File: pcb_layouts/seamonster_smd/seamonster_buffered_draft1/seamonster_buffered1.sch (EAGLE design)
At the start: 84 parts, among them IC1 7805T, IC2 4051D, IC3 4051D, IC4 DG408DY, IC5 4040D, IC6 40106D, IC7 4070D, Q1 THONKICONNNEW, Q2 THONKICONNNEW, Q3 THONKICONNNEW, Q4 THONKICONNNEW, Q5 THONKICONNNEW, Q6 THONKICONNNEW, SW1 T-80-T-SPDT-ON-OFF-ON, SW2 T-80-T-SPDT-ON-OFF-ON, SW3 T-80-T-SPDT-ON-OFF-ON, SW4 T-80-T-SPDT-ON-OFF-ON

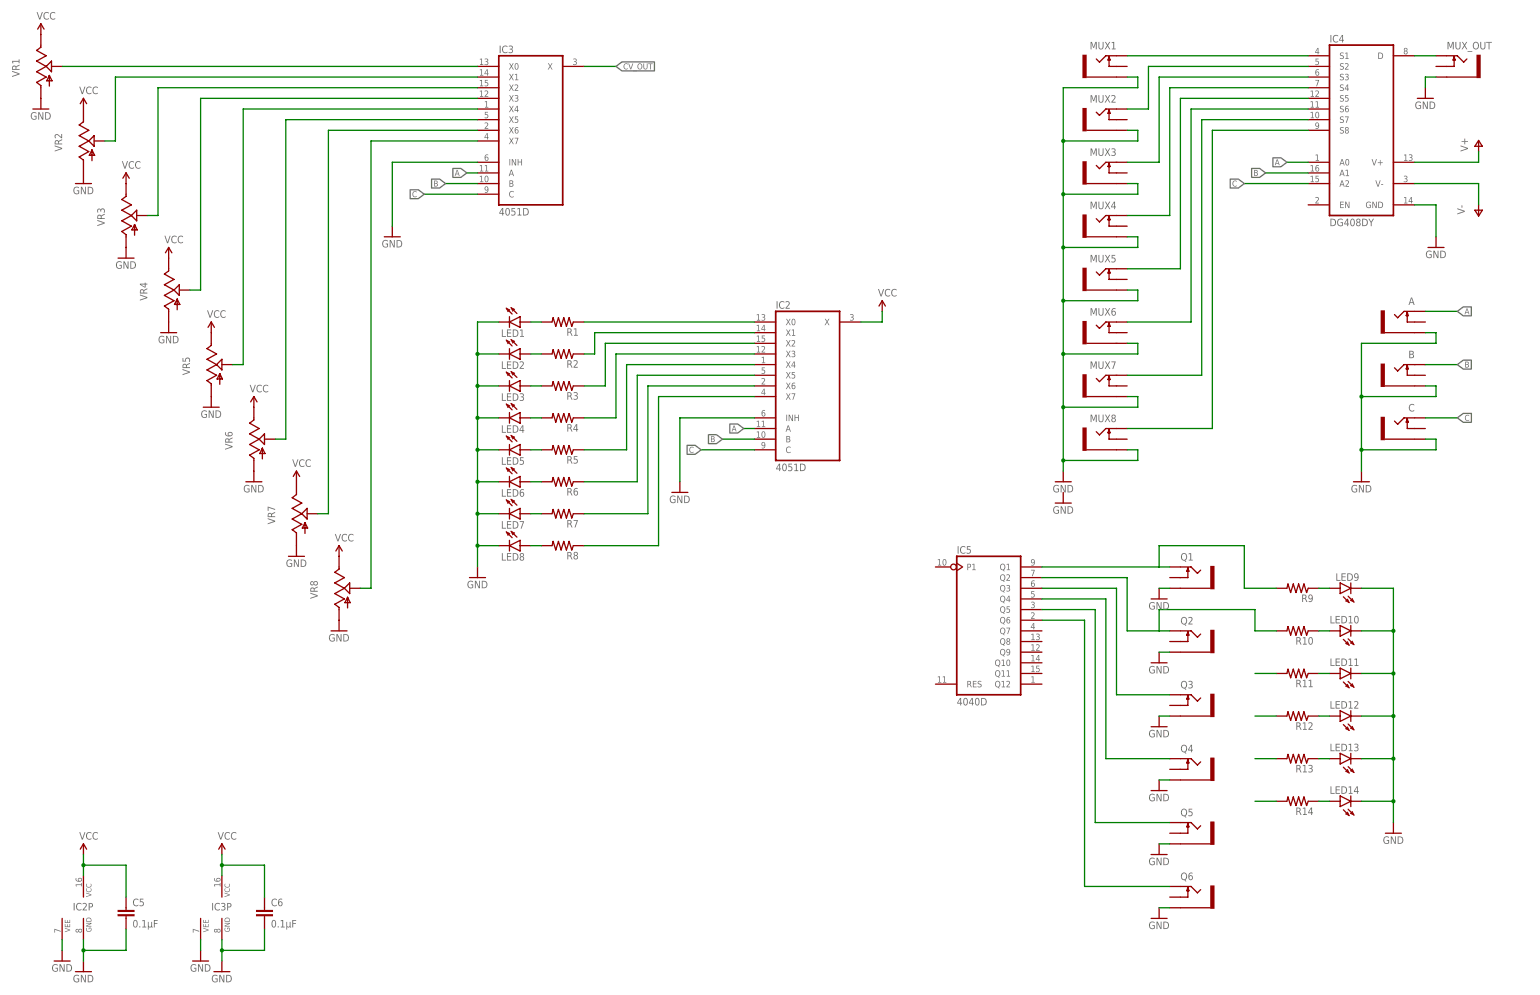
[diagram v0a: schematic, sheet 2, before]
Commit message: figured out invoking across multiple sheets
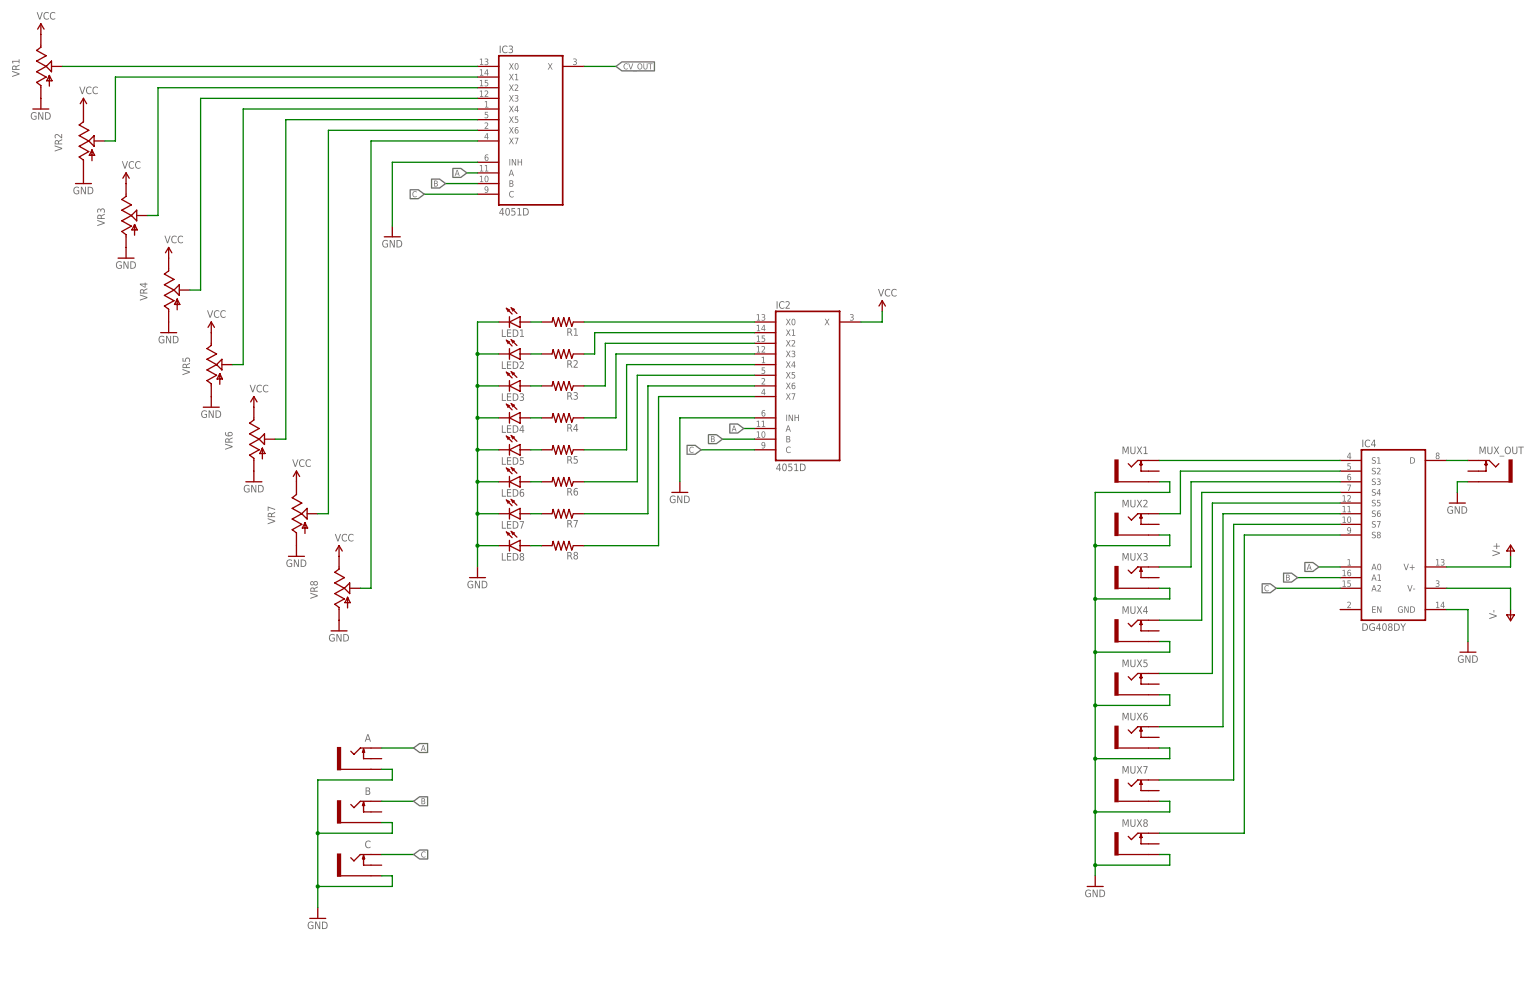
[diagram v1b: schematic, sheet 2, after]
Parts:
- removed IC5: 4040D, 40xx:4040D
- removed LED10, LED11, LED12, LED13, LED14, LED9: (no value), SparkFun-LED:LED3MM
- removed Q1, Q2, Q3, Q4, Q5, Q6: THONKICONNNEW, MusicThingModular:THONKICONNNEW
- removed R10, R11, R12, R13, R14, R9: (no value), SparkFun-Resistors:RESISTOR0805-RES
- added U1: TL084, MusicThingModular:TL074_SMD
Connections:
- removed net N$34: LED9.A, R9.1
- removed net N$35: LED10.A, R10.1
- removed net N$36: LED11.A, R11.1
- removed net N$37: LED12.A, R12.1
- removed net N$38: LED13.A, R13.1
- removed net N$39: LED14.A, R14.1
- removed net N$40: IC5A.Q1, Q1.TIP, R9.2
- removed net N$41: IC5A.Q2, Q2.TIP, R10.2
- removed net N$42: IC5A.Q3, Q3.TIP
- removed net N$43: IC5A.Q4, Q4.TIP
- removed net N$44: IC5A.Q5, Q5.TIP
- removed net N$45: IC5A.Q6, Q6.TIP
- removed net N$48: R11.2
- removed net N$49: R12.2
- removed net N$50: R13.2
- removed net N$51: R14.2
- new net CCO1_BUFFERED: U1A.-IN, U1A.OUT
- new net CCO2_BUFFERED: U1B.-IN, U1B.OUT
- new net CCO3_BUFFERED: U1C.-IN, U1C.OUT
- new net CCO4_BUFFERED: U1D.-IN, U1D.OUT
- net CCO1: now also U1A.+IN
- net GND: no longer IC2P.GND, IC2P.VEE, IC3P.GND, IC3P.VEE, LED10.C, LED11.C, LED12.C, LED13.C, LED14.C, LED9.C, Q1.SLEEVE, Q2.SLEEVE, Q3.SLEEVE, Q4.SLEEVE, Q5.SLEEVE, Q6.SLEEVE
- net N$54: now also U1B.+IN
- net N$57: now also U1C.+IN
- net N$61: now also U1D.+IN
- net V+: now also C5.1, U1P.V+
- net V-: now also C6.1, U1P.V-
- net VCC: no longer C5.1, C6.1, IC2P.VCC, IC3P.VCC
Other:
- moved on the sheet: A, B, C, C1, C2, C3, C4, IC1, IC4, IC6F, IC7A, IC7B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

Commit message: fleshed out schematic pages
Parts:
- added C15, C16, C17, C18, C19, C20: 0.1µF, SparkFun-Capacitors:CAP0805
- added IC5, IC8: 4046D, 40xx:4046D
- added U2: TL084, MusicThingModular:TL074_SMD
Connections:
- new net COMPLEX_OUT1_BUFFERED: U2A.-IN, U2A.OUT
- new net COMPLEX_OUT2_BUFFERED: U2B.-IN, U2B.OUT
- new net N$34: IC7A.I0
- new net N$35: IC7A.O, IC7B.I0
- new net N$36: IC7C.O, IC7D.I0
- new net N$37: IC7C.I0
- new net N$38: IC7B.O, U2A.+IN
- new net N$39: IC7D.O, U2B.+IN
- net CCO1_BUFFERED: now also IC7A.I1
- net CCO2_BUFFERED: now also IC7B.I1
- net CCO3_BUFFERED: now also IC7C.I1
- net CCO4_BUFFERED: now also IC7D.I1
- net GND: now also C15.2, C16.2, C17.2, C18.2, C19.2, C20.2, IC2P.GND, IC2P.VEE, IC3P.GND, IC3P.VEE, IC6P.VSS, IC7P.VSS
- net V+: now also C18.1, U2P.V+
- net V-: now also C19.1, U2P.V-
- net VCC: now also C15.1, C16.1, C17.1, C20.1, IC2P.VCC, IC3P.VCC, IC6P.VDD, IC7P.VDD

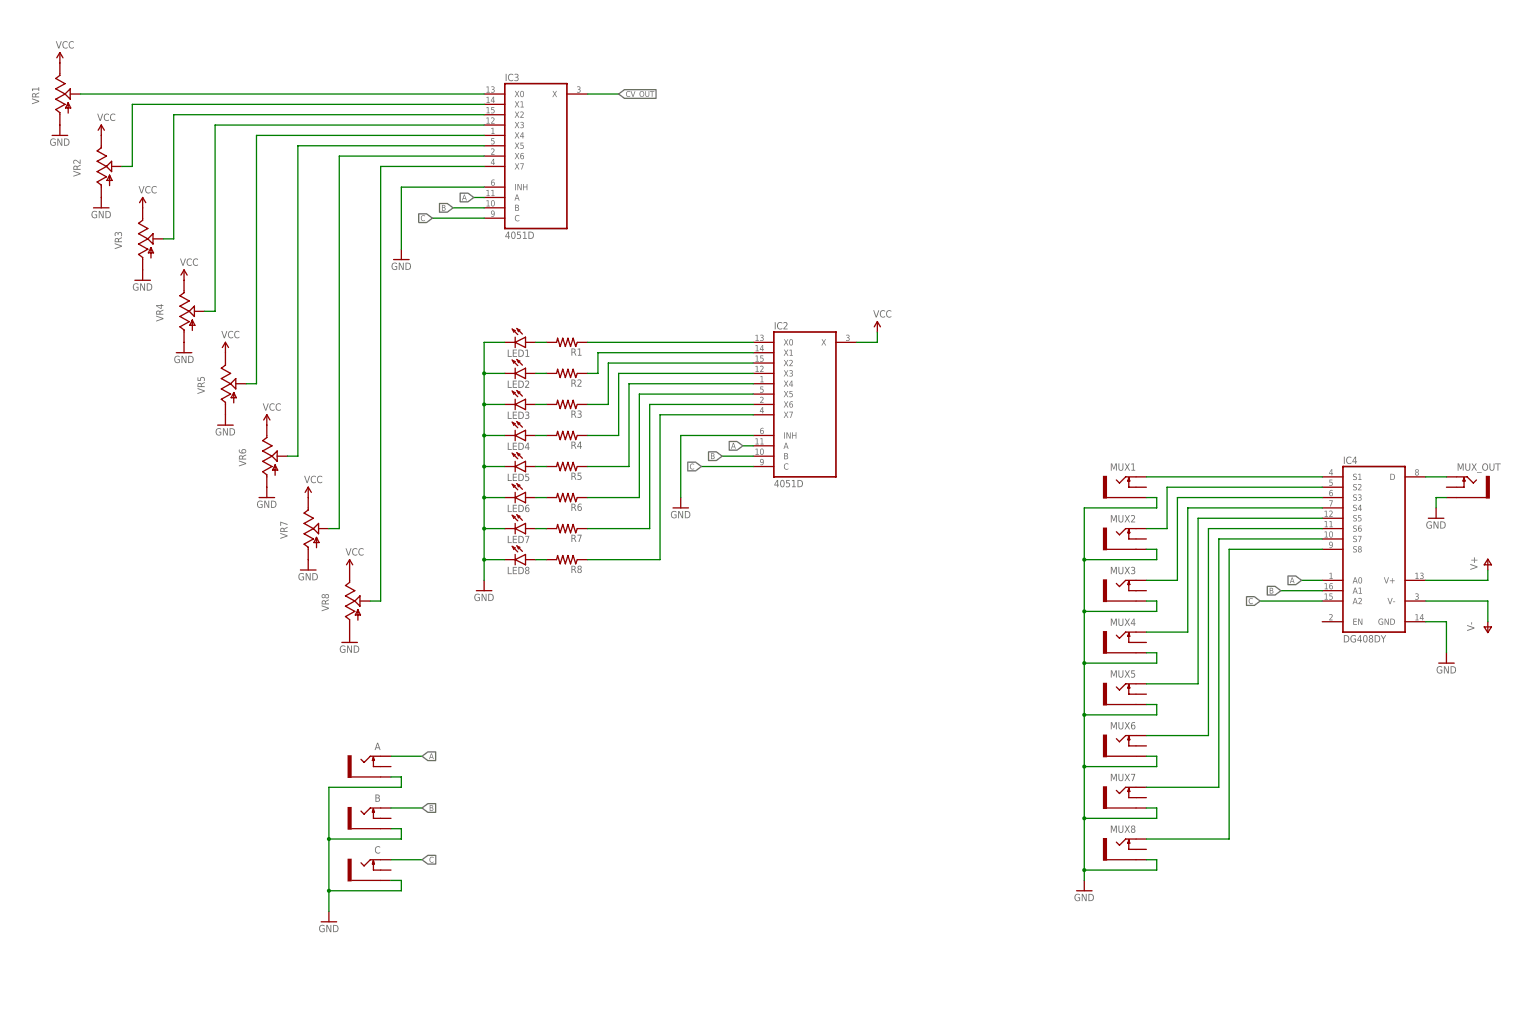
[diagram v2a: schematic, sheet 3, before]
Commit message: added in VCOs and more buffering
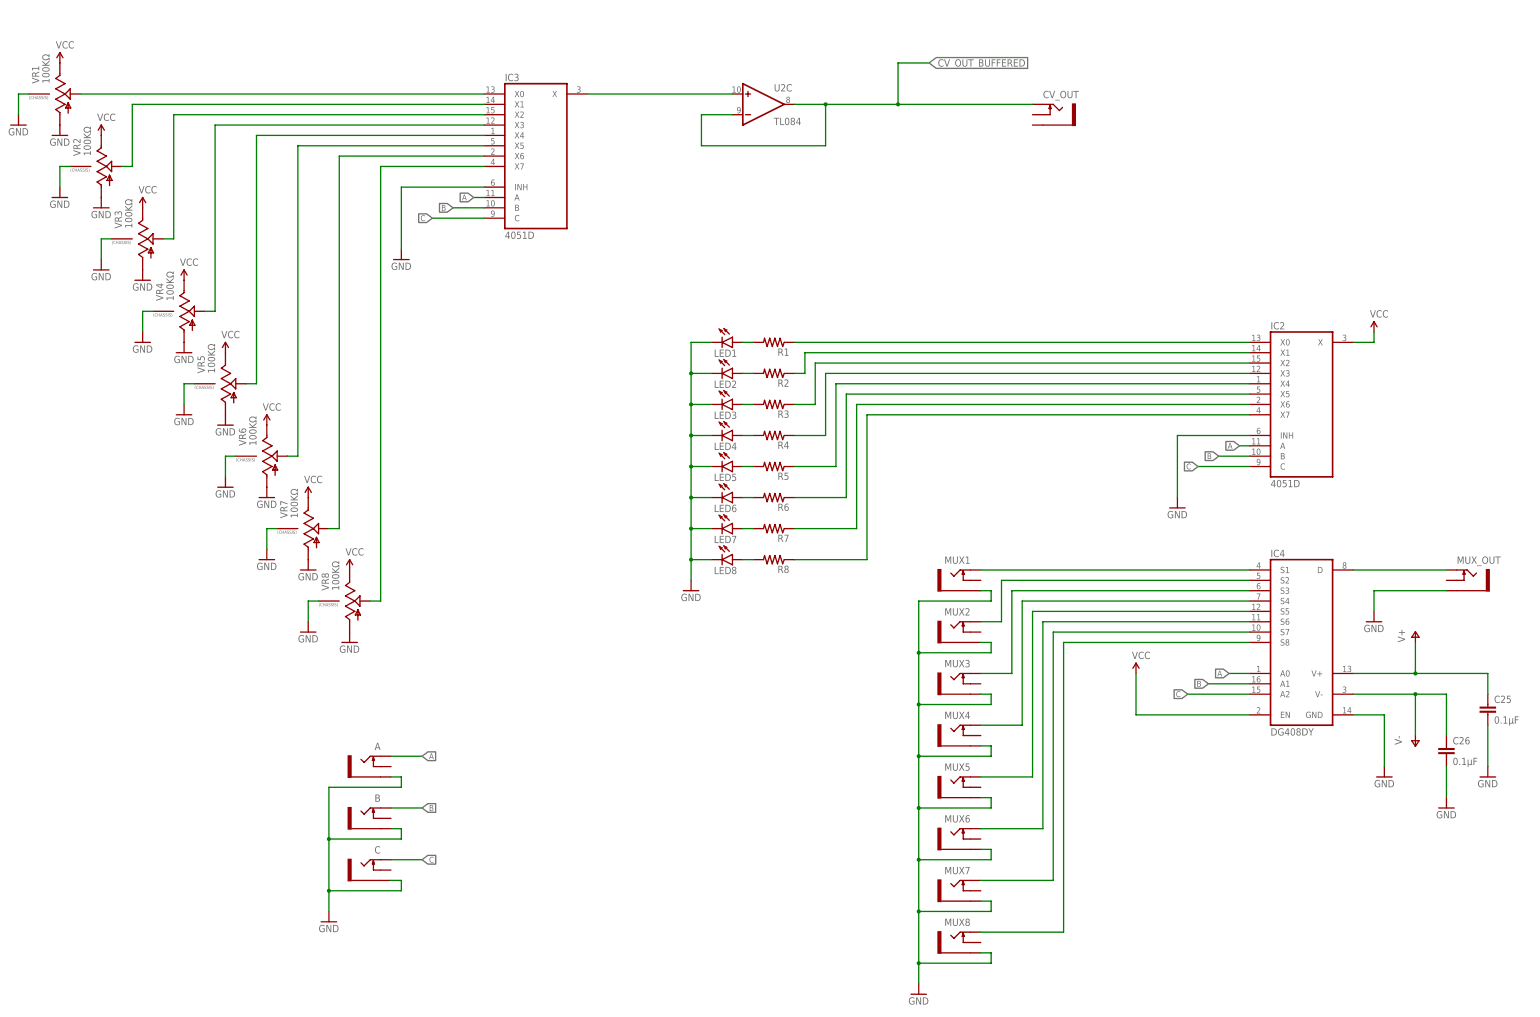
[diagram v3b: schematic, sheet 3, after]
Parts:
- added C21, C22, C25, C26, C27, C28, C29: 0.1µF, SparkFun-Capacitors:CAP0805
- added C23, C24: 1µF, SparkFun-Capacitors:CAP0805
- added CLOCK_IN, CV_OUT, Q1, Q2, Q3, Q4, Q5, Q6: THONKICONNNEW, MusicThingModular:THONKICONNNEW
- added CLOCK_SELECT: T-80-T-SPDT-ON-OFF-ON, MusicThingModular:T-80-T-SPDT-ON-OFF-ON
- added IC9: 4040D, 40xx:4040D
- added LED10, LED11, LED12, LED13, LED14, LED9: (no value), SparkFun-LED:LED3MM
- added R10, R11, R12, R13, R14, R15, R16, R17, R18, R9: (no value), SparkFun-Resistors:RESISTOR0805-RES
- added U3: TL084, MusicThingModular:TL074_SMD
- added VR13, VR14: 1MΩ, MusicThingModular:9MM_SNAP-IN_POT_CHASSIS
- added VR15: 100KΩ, MusicThingModular:9MM_SNAP-IN_POT_CHASSIS
- VR1, VR10, VR11, VR12, VR2, VR3, VR4, VR5, VR6, VR7, VR8: value (none) -> 100KΩ; device MusicThingModular:9MM_SNAP-IN_POT_ -> MusicThingModular:9MM_SNAP-IN_POT_CHASSIS
- VR9: device MusicThingModular:9MM_SNAP-IN_POT_ -> MusicThingModular:9MM_SNAP-IN_POT_CHASSIS
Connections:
- new net CV_OUT_BUFFERED: CV_OUT.TIP, IC5A.VCOIN, IC8A.VCOIN, U2C.-IN, U2C.OUT
- new net N$40: IC5A.R2, R15.2
- new net N$41: IC6A.I, VR15.A
- new net N$42: R15.1, VR13.E
- new net N$43: CLOCK_SELECT.S, IC6A.O, VR15.S
- new net N$44: C23.1, IC5A.CX@1
- new net N$45: C23.2, IC5A.CX@2
- new net N$48: C24.1, IC8A.CX@1
- new net N$49: C24.2, IC8A.CX@2
- new net N$50: CLOCK_SELECT.P, IC9A.P1
- new net N$51: LED9.A, R9.2
- new net N$65: LED10.A, R10.2
- new net N$66: LED11.A, R11.2
- new net N$67: LED12.A, R12.2
- new net N$68: LED13.A, R13.2
- new net N$69: LED14.A, R14.2
- new net N$70: CLOCK_IN.TIP, CLOCK_SELECT.O
- new net N$71: IC8A.R2, R16.2
- new net N$72: R16.1, VR14.E
- new net N$74: IC8A.R1, R18.2
- new net N$75: IC5A.R1, R17.2
- new net Q1: IC9A.Q1, Q1.TIP, R9.1
- new net Q2: IC9A.Q2, Q2.TIP, R10.1
- new net Q3: IC9A.Q3, Q3.TIP, R11.1
- new net Q4: IC9A.Q4, Q4.TIP, R12.1
- new net Q5: IC9A.Q5, Q5.TIP, R13.1
- new net Q6: IC9A.Q6, Q6.TIP, R14.1
- new net VCO1_OUT: IC5A.VCOOUT, U3A.+IN
- new net VCO1_OUT_BUFFERED: U3A.-IN, U3A.OUT
- new net VCO2_OUT: IC8A.VCOOUT, U3B.+IN
- new net VCO2_OUT_BUFFERED: U3B.-IN, U3B.OUT
- net CV_OUT: now also U2C.+IN
- net GND: now also C21.2, C22.2, C25.2, C26.2, C27.2, C28.2, C29.2, CLOCK_IN.SLEEVE, IC5A.INH, IC5P.VSS, IC8A.INH, IC8P.VSS, IC9A.RES, IC9P.VSS, LED10.C, LED11.C, LED12.C, LED13.C, LED14.C, LED9.C, Q1.SLEEVE, Q2.SLEEVE, Q3.SLEEVE, Q4.SLEEVE, Q5.SLEEVE, Q6.SLEEVE, R17.1, R18.1, VR1.P$1, VR10.P$1, VR11.P$1, VR12.P$1, VR13.P$1, VR13.S, VR14.P$1, VR14.S, VR15.P$1, VR2.P$1, VR3.P$1, VR4.P$1, VR5.P$1, VR6.P$1, VR7.P$1, VR8.P$1, VR9.P$1
- net V+: now also C25.1, C28.1, U3P.V+
- net V-: now also C26.1, C29.1, U3P.V-
- net VCC: now also C21.1, C22.1, C27.1, IC4.EN, IC5P.VDD, IC8P.VDD, IC9P.VDD
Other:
- moved on the sheet: IC2, IC4, IC6A, LED1, LED2, LED3, LED4, LED5, LED6, LED7, LED8, MUX1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

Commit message: roughly positioned thruhole panel parts
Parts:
- added CCO1, CCO2, CCO3, CCO4, COMPLEX1, COMPLEX2, VCO1, VCO2: THONKICONNNEW, MusicThingModular:THONKICONNNEW
- CLOCK_SELECT, SW1, SW2, SW3, SW4: value T-80-T-SPDT-ON-OFF-ON -> SPDT ON-ON
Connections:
- new net N$73: CCO1.SLEEVE, CCO2.SLEEVE, CCO3.SLEEVE, CCO4.SLEEVE, COMPLEX1.SLEEVE, COMPLEX2.SLEEVE
- net CCO1_BUFFERED: now also CCO1.TIP
- net CCO2_BUFFERED: now also CCO2.TIP
- net CCO3_BUFFERED: now also CCO3.TIP
- net CCO4_BUFFERED: now also CCO4.TIP
- net COMPLEX_OUT1_BUFFERED: now also COMPLEX1.TIP
- net COMPLEX_OUT2_BUFFERED: now also COMPLEX2.TIP
- net GND: now also CV_OUT.SLEEVE, VCO1.SLEEVE, VCO2.SLEEVE
- net VCO1_OUT_BUFFERED: now also VCO1.TIP
- net VCO2_OUT_BUFFERED: now also VCO2.TIP
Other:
- moved on the sheet: U2A, U2B

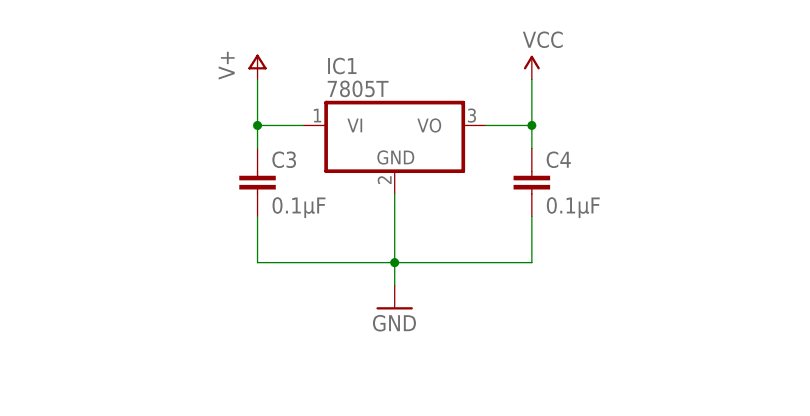
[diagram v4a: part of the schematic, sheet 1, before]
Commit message: roughly placed all remaining parts
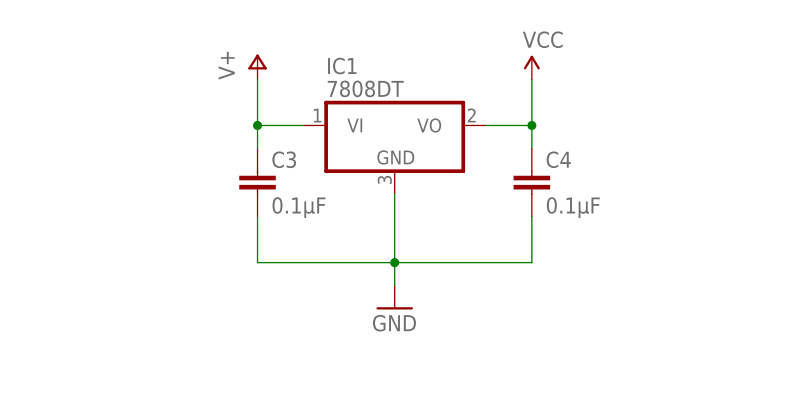
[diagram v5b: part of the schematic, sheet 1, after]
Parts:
- IC1: value 7805T -> 7808DT; device linear:7805T -> linear:7808DT
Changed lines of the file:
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@@
 <parts>
 <part name="U$1" library="combo_power" deviceset="COMBO_POWER" device=""/>
-<part name="IC1" library="linear" library_urn="urn:adsk.eagle:library:262" deviceset="78*" device="T" technology="05"/>
 <part name="C1" library="SparkFun-Capacitors" deviceset="CAP_POL" device="PTH2" value="47µF"/>
 <part name="C2" library="SparkFun-Capacitors" deviceset="CAP_POL" device="PTH2" value="47µF"/>
@@
 <part name="GND72" library="supply1" library_urn="urn:adsk.eagle:library:371" deviceset="GND" device=""/>
 <part name="GND73" library="supply1" library_urn="urn:adsk.eagle:library:371" deviceset="GND" device=""/>
+<part name="IC1" library="linear" library_urn="urn:adsk.eagle:library:262" deviceset="78*" device="DT" technology="08"/>
 </parts>
 <sheets>
@@
 <instances>
 <instance part="U$1" gate="G$1" x="27.94" y="223.52"/>
-<instance part="IC1" gate="A1" x="111.76" y="231.14"/>
 <instance part="C1" gate="G$1" x="170.18" y="231.14"/>
 <instance part="C2" gate="G$1" x="200.66" y="231.14"/>
@@
 <instance part="GND68" gate="1" x="170.18" y="68.58"/>
 <instance part="GND69" gate="1" x="170.18" y="43.18"/>
+<instance part="IC1" gate="A1" x="111.76" y="231.14"/>
 </instances>
 <busses>
@@
 </segment>
 <segment>
-<pinref part="IC1" gate="A1" pin="VI"/>
 <pinref part="P+3" gate="1" pin="V+"/>
 <wire x1="101.6" y1="231.14" x2="96.52" y2="231.14" width="0.1524" layer="91"/>
@@
 <wire x1="96.52" y1="231.14" x2="96.52" y2="228.6" width="0.1524" layer="91"/>
 <junction x="96.52" y="231.14"/>
+<pinref part="IC1" gate="A1" pin="VI"/>
 </segment>
 <segment>
@@
 </segment>
 <segment>
-<pinref part="IC1" gate="A1" pin="GND"/>
 <pinref part="GND4" gate="1" pin="GND"/>
 <wire x1="111.76" y1="223.52" x2="111.76" y2="215.9" width="0.1524" layer="91"/>
@@
 <wire x1="127" y1="215.9" x2="111.76" y2="215.9" width="0.1524" layer="91"/>
 <junction x="111.76" y="215.9"/>
+<pinref part="IC1" gate="A1" pin="GND"/>
 </segment>
 <segment>
@@
 <net name="VCC" class="0">
 <segment>
-<pinref part="IC1" gate="A1" pin="VO"/>
 <wire x1="121.92" y1="231.14" x2="127" y2="231.14" width="0.1524" layer="91"/>
 <pinref part="SUPPLY1" gate="G$1" pin="VCC"/>
@@
 <wire x1="127" y1="231.14" x2="127" y2="228.6" width="0.1524" layer="91"/>
 <junction x="127" y="231.14"/>
-</segment>
-<segment>
+<pinref part="IC1" gate="A1" pin="VO"/>
+</segment>
+<segment>
